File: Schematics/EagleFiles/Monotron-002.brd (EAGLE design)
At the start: 88 x 38.5 mm, 52 parts, among them IC1 LM324D, J1 pitch_CV, J2 gate_CV, J3 cutoff_CV, J4 LFO, Q1 N-MOSFET, U1 TPS2105D, X1 MICRO-USB-RECEPTACLE47589-0001

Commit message: updated schematics and brd files
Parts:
- R2: value 47k -> 10k
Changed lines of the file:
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@@
 <drawing>
 <settings>
-<setting alwaysvectorfont="yes"/>
+<setting alwaysvectorfont="no"/>
 <setting verticaltext="up"/>
 </settings>
@@
 <attribute name="VALUE" x="49.405" y="11.865" size="1.27" layer="27" rot="R90"/>
 </element>
-<element name="R2" library="Mage-Control" package="R0603" value="47k" x="44.5" y="12.5" smashed="yes" rot="R270">
+<element name="R2" library="Mage-Control" package="R0603" value="10k" x="44.5" y="12.5" smashed="yes" rot="R270">
 <attribute name="NAME" x="44.135" y="10.835" size="0.8128" layer="25" font="vector" ratio="15" rot="R270"/>
 <attribute name="VALUE" x="42.595" y="13.135" size="1.27" layer="27" rot="R270"/>

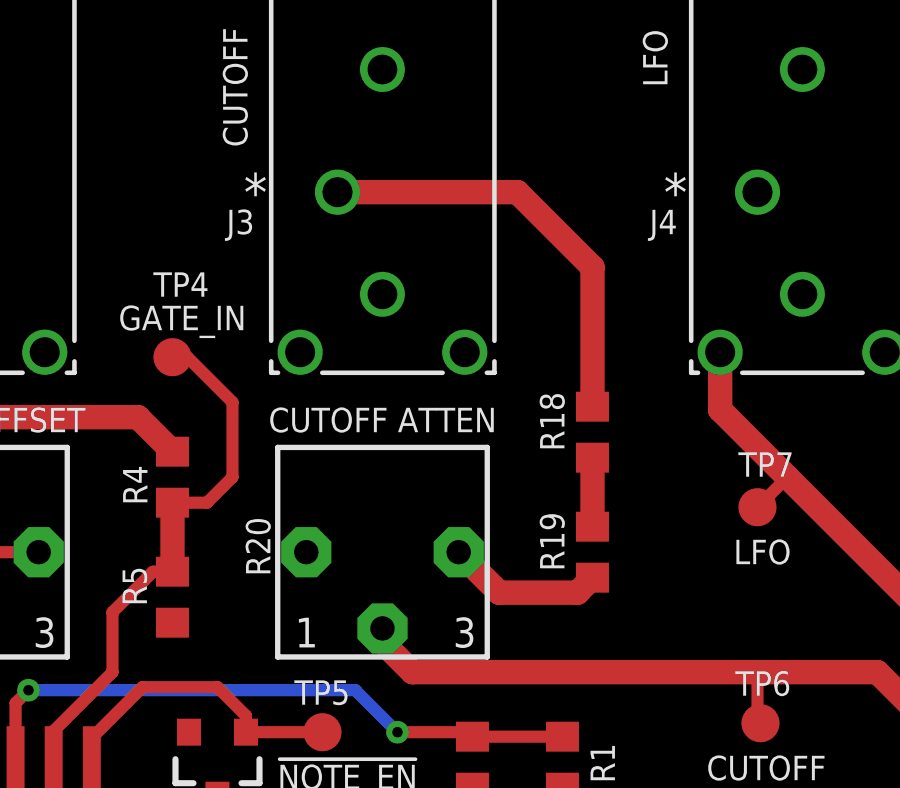
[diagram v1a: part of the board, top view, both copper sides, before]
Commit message: updated eagle files
corrected cutoff connector wiring and cutoff trimmer disconnected from GND
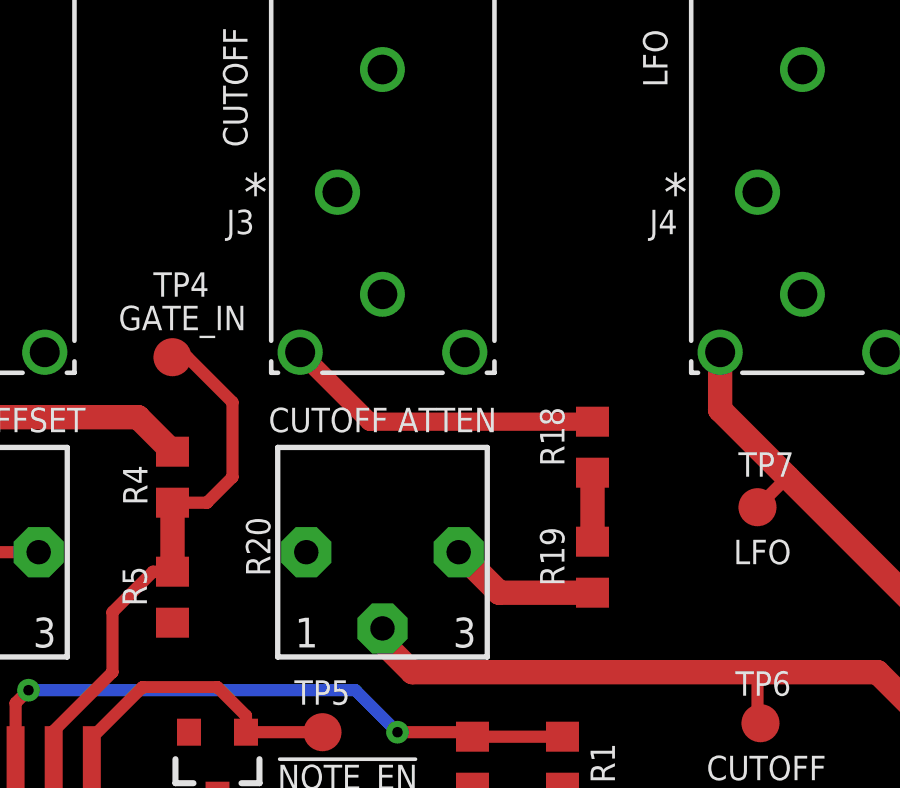
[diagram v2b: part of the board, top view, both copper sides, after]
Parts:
- moved R18 0.50 mm to (48.5, 23.0)
- moved R19 0.50 mm to (48.5, 19.0)
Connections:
- removed net N$8: J3.1, R18.2
- new net N$6: J3.3, R18.2
- net GND: now also J3.1; no longer J3.3, R20.1
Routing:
- net N$8: track 14.2 -> 0.00 mm
- net N$6: track 0.00 -> 10.7 mm
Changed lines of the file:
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@@
 <attribute name="VALUE" x="32.595" y="18.635" size="1.27" layer="27" rot="R270"/>
 </element>
-<element name="R18" library="Mage-Control" package="R0603" value="68k" x="48.5" y="23.5" smashed="yes" rot="R90">
-<attribute name="NAME" x="47.565" y="22.865" size="0.8128" layer="25" font="vector" ratio="15" rot="R90"/>
-<attribute name="VALUE" x="50.405" y="22.865" size="1.27" layer="27" rot="R90"/>
-</element>
-<element name="R19" library="Mage-Control" package="R0603" value="68k" x="48.5" y="19.5" smashed="yes" rot="R90">
-<attribute name="NAME" x="47.565" y="18.865" size="0.8128" layer="25" font="vector" ratio="15" rot="R90"/>
-<attribute name="VALUE" x="50.405" y="18.865" size="1.27" layer="27" rot="R90"/>
+<element name="R18" library="Mage-Control" package="R0603" value="68k" x="48.5" y="23" smashed="yes" rot="R90">
+<attribute name="NAME" x="47.565" y="22.365" size="0.8128" layer="25" font="vector" ratio="15" rot="R90"/>
+<attribute name="VALUE" x="50.405" y="22.365" size="1.27" layer="27" rot="R90"/>
+</element>
+<element name="R19" library="Mage-Control" package="R0603" value="68k" x="48.5" y="19" smashed="yes" rot="R90">
+<attribute name="NAME" x="47.565" y="18.365" size="0.8128" layer="25" font="vector" ratio="15" rot="R90"/>
+<attribute name="VALUE" x="50.405" y="18.365" size="1.27" layer="27" rot="R90"/>
 </element>
 <element name="C1" library="Mage-Control" package="C0603" value="1n" x="26.5" y="3.5" smashed="yes" rot="R90">
@@
 <contactref element="J1" pad="2"/>
 <contactref element="R17" pad="2"/>
-<contactref element="J3" pad="2"/>
-<contactref element="J3" pad="3"/>
 <contactref element="J2" pad="2"/>
 <contactref element="J2" pad="1"/>
@@
 <contactref element="C4" pad="1"/>
 <contactref element="IC1" pad="11"/>
-<contactref element="R20" pad="1"/>
 <contactref element="R13" pad="1"/>
 <contactref element="R5" pad="2"/>
@@
 <via x="43" y="9.5" extent="1-16" drill="0.35"/>
 <via x="44.5" y="9.5" extent="1-16" drill="0.35"/>
+<contactref element="J3" pad="1"/>
+<contactref element="J3" pad="2"/>
 </signal>
 <signal name="VCC_USB">
@@
 <wire x1="54.3" y1="6.95" x2="54" y2="6.65" width="0.4064" layer="1"/>
 </signal>
-<signal name="N$8">
-<contactref element="J3" pad="1"/>
-<contactref element="R18" pad="2"/>
-<wire x1="40" y1="31.5" x2="46" y2="31.5" width="0.8128" layer="1"/>
-<wire x1="48.5" y1="29" x2="48.5" y2="24.35" width="0.8128" layer="1"/>
-<wire x1="46" y1="31.5" x2="48.5" y2="29" width="0.8128" layer="1"/>
-</signal>
 <signal name="N$9">
 <contactref element="R18" pad="1"/>
 <contactref element="R19" pad="2"/>
-<wire x1="48.5" y1="20.35" x2="48.5" y2="22.65" width="0.8128" layer="1"/>
+<wire x1="48.5" y1="19.85" x2="48.5" y2="22.15" width="0.8128" layer="1"/>
 </signal>
 <signal name="N$10">
 <contactref element="R20" pad="3"/>
 <contactref element="R19" pad="1"/>
-<wire x1="48.5" y1="18.65" x2="48" y2="18.15" width="0.8128" layer="1"/>
-<wire x1="48" y1="18.15" x2="45.39" y2="18.15" width="0.8128" layer="1"/>
+<wire x1="48.5" y1="18.15" x2="45.39" y2="18.15" width="0.8128" layer="1"/>
 <wire x1="45.39" y1="18.15" x2="44.04" y2="19.5" width="0.8128" layer="1"/>
 </signal>
@@
 <wire x1="36.5" y1="8.5" x2="36.5" y2="8.35" width="0.4064" layer="1"/>
 </signal>
+<signal name="N$6">
+<contactref element="R18" pad="2"/>
+<contactref element="J3" pad="3"/>
+<wire x1="38.7554" y1="26.166" x2="41.0714" y2="23.85" width="0.6096" layer="1"/>
+<wire x1="41.0714" y1="23.85" x2="48.5" y2="23.85" width="0.6096" layer="1"/>
+</signal>
 </signals>
